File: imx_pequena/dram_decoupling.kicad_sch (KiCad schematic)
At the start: 19 parts

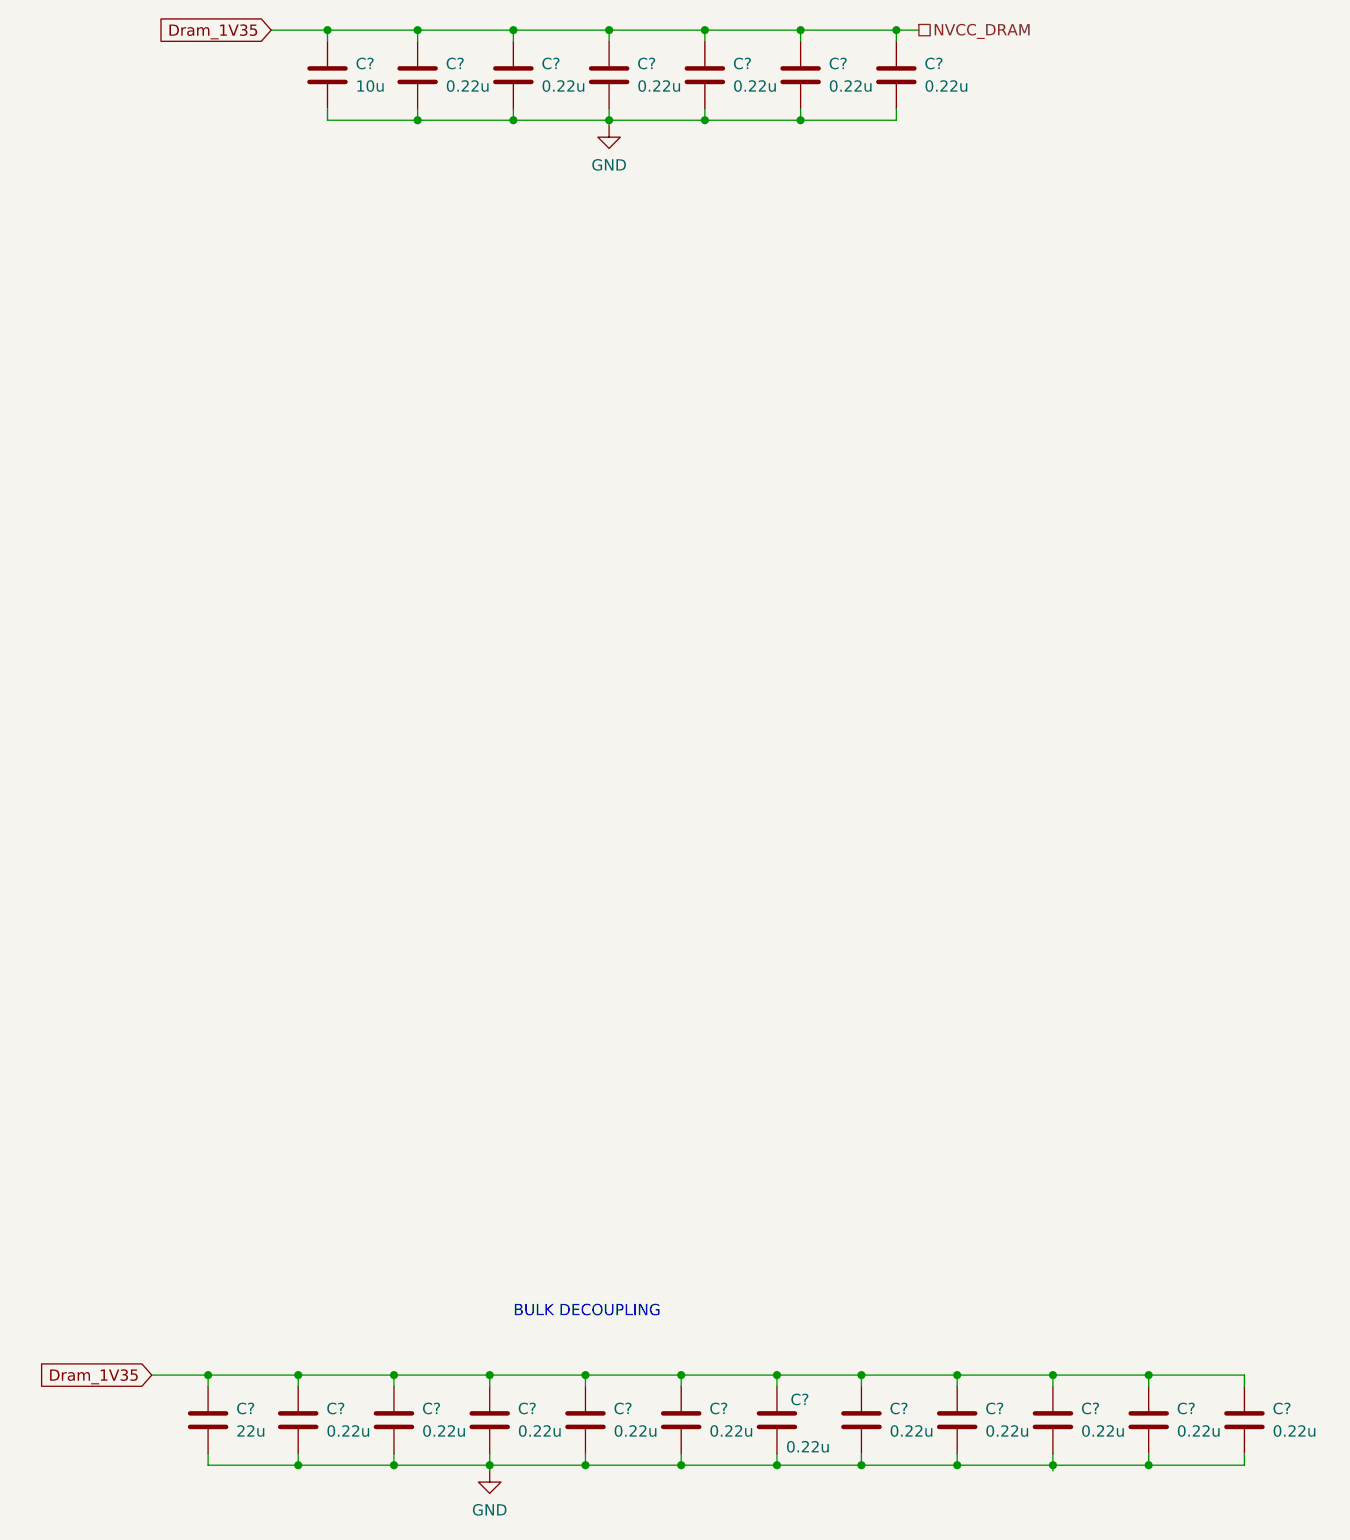
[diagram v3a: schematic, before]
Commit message: Power Update
Added 3v3 and 1.35V switchers
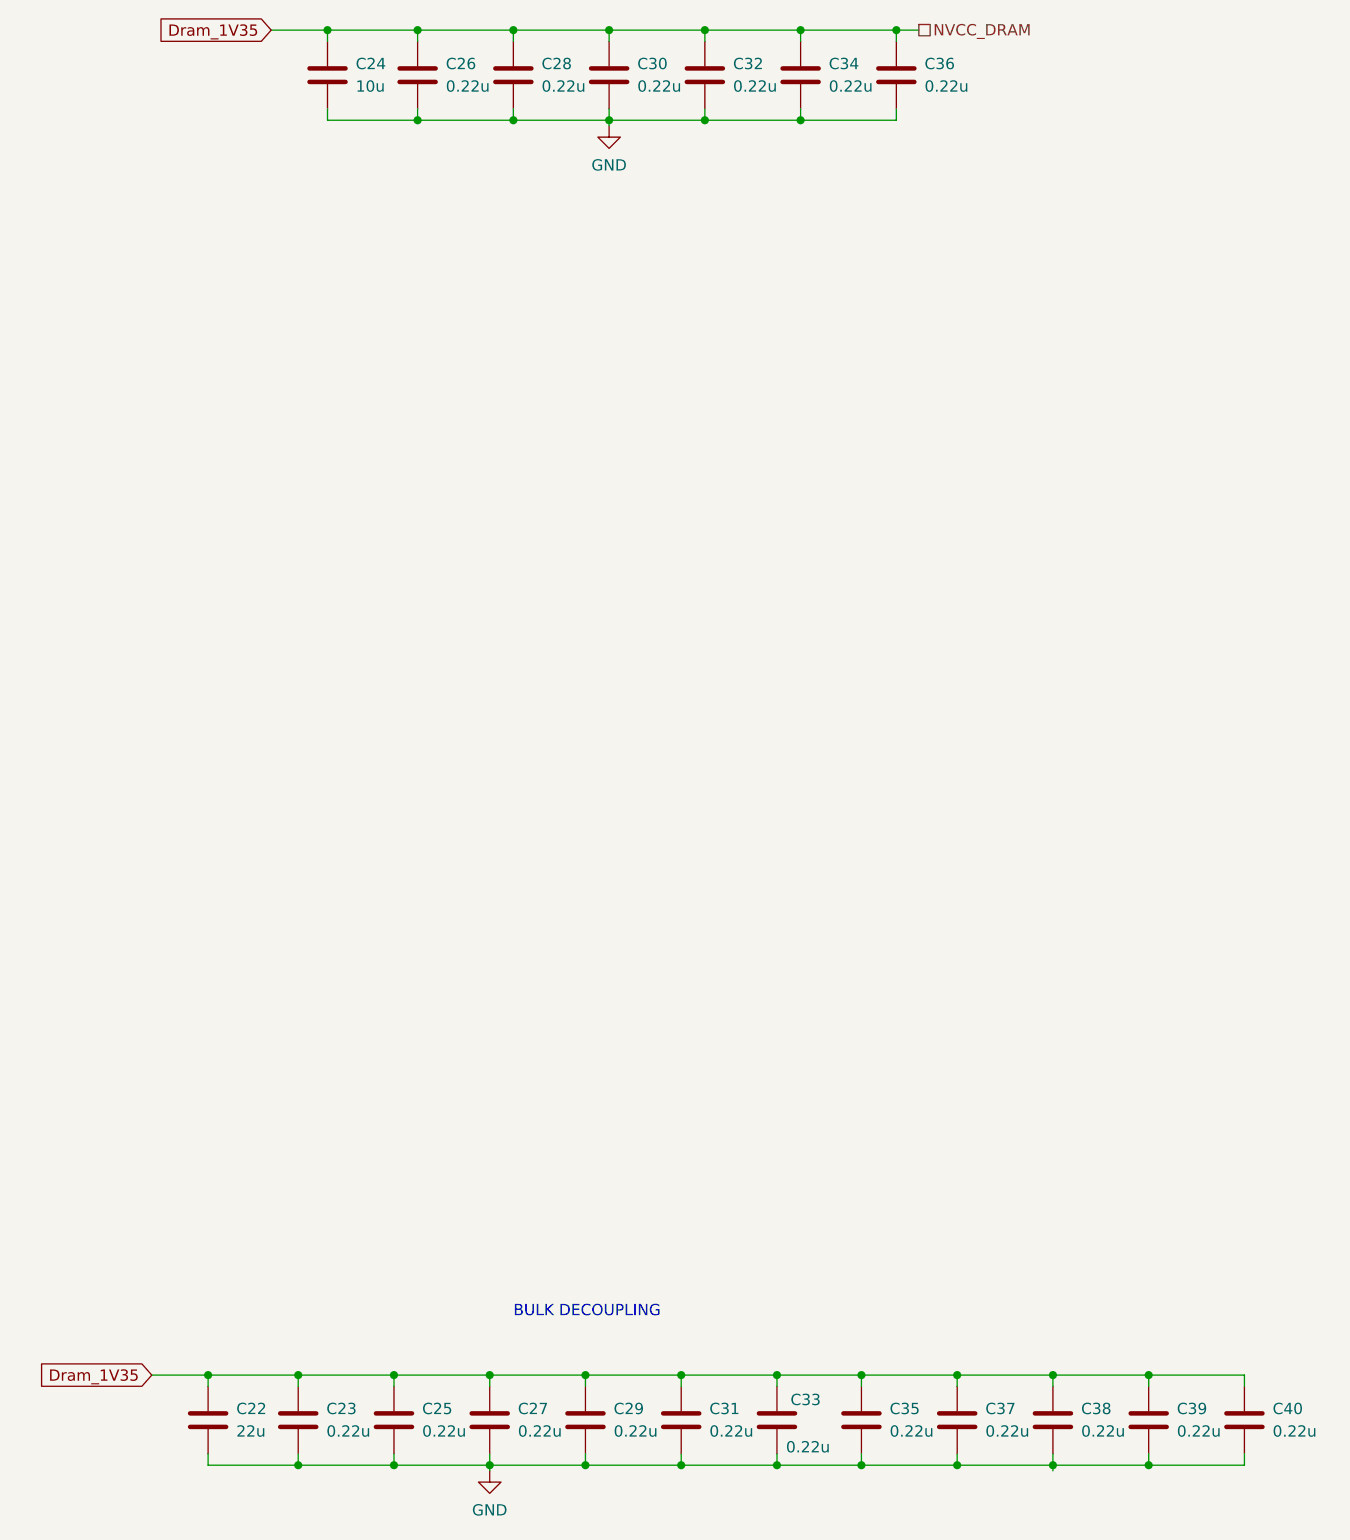
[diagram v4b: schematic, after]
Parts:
- gave numbers to parts that had none: 19
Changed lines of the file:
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@@
   (symbol (lib_id "Device:C") (at 55.118 184.658 0) (unit 1)
     (in_bom yes) (on_board yes) (fields_autoplaced)
-    (property "Reference" "C?" (id 0) (at 58.293 183.3879 0)
+    (property "Reference" "C25" (id 0) (at 58.293 183.3879 0)
       (effects (font (size 1.27 1.27)) (justify left))
     )
@@
   (symbol (lib_id "Device:C") (at 79.375 33.02 0) (unit 1)
     (in_bom yes) (on_board yes) (fields_autoplaced)
-    (property "Reference" "C?" (id 0) (at 82.55 31.7499 0)
+    (property "Reference" "C30" (id 0) (at 82.55 31.7499 0)
       (effects (font (size 1.27 1.27)) (justify left))
     )
@@
   (symbol (lib_id "Device:C") (at 76.708 184.658 0) (unit 1)
     (in_bom yes) (on_board yes) (fields_autoplaced)
-    (property "Reference" "C?" (id 0) (at 79.883 183.3879 0)
+    (property "Reference" "C29" (id 0) (at 79.883 183.3879 0)
       (effects (font (size 1.27 1.27)) (justify left))
     )
@@
   (symbol (lib_id "Device:C") (at 90.17 33.02 0) (unit 1)
     (in_bom yes) (on_board yes) (fields_autoplaced)
-    (property "Reference" "C?" (id 0) (at 93.345 31.7499 0)
+    (property "Reference" "C32" (id 0) (at 93.345 31.7499 0)
       (effects (font (size 1.27 1.27)) (justify left))
     )
@@
   (symbol (lib_id "power:GND") (at 65.913 190.373 0) (unit 1)
     (in_bom yes) (on_board yes) (fields_autoplaced)
-    (property "Reference" "#PWR?" (id 0) (at 65.913 196.723 0)
+    (property "Reference" "#PWR0122" (id 0) (at 65.913 196.723 0)
       (effects (font (size 1.27 1.27)) hide)
     )
@@
   (symbol (lib_id "Device:C") (at 65.913 184.658 0) (unit 1)
     (in_bom yes) (on_board yes) (fields_autoplaced)
-    (property "Reference" "C?" (id 0) (at 69.088 183.3879 0)
+    (property "Reference" "C27" (id 0) (at 69.088 183.3879 0)
       (effects (font (size 1.27 1.27)) (justify left))
     )
@@
   (symbol (lib_id "power:GND") (at 79.375 38.735 0) (unit 1)
     (in_bom yes) (on_board yes) (fields_autoplaced)
-    (property "Reference" "#PWR?" (id 0) (at 79.375 45.085 0)
+    (property "Reference" "#PWR0121" (id 0) (at 79.375 45.085 0)
       (effects (font (size 1.27 1.27)) hide)
     )
@@
   (symbol (lib_id "Device:C") (at 129.413 184.658 0) (unit 1)
     (in_bom yes) (on_board yes) (fields_autoplaced)
-    (property "Reference" "C?" (id 0) (at 132.588 183.3879 0)
+    (property "Reference" "C38" (id 0) (at 132.588 183.3879 0)
       (effects (font (size 1.27 1.27)) (justify left))
     )
@@
   (symbol (lib_id "Device:C") (at 151.003 184.658 0) (unit 1)
     (in_bom yes) (on_board yes) (fields_autoplaced)
-    (property "Reference" "C?" (id 0) (at 154.178 183.3879 0)
+    (property "Reference" "C40" (id 0) (at 154.178 183.3879 0)
       (effects (font (size 1.27 1.27)) (justify left))
     )
@@
   (symbol (lib_id "Device:C") (at 98.298 184.658 0) (unit 1)
     (in_bom yes) (on_board yes)
-    (property "Reference" "C?" (id 0) (at 99.822 182.372 0)
+    (property "Reference" "C33" (id 0) (at 99.822 182.372 0)
       (effects (font (size 1.27 1.27)) (justify left))
     )
@@
   (symbol (lib_id "Device:C") (at 111.76 33.02 0) (unit 1)
     (in_bom yes) (on_board yes) (fields_autoplaced)
-    (property "Reference" "C?" (id 0) (at 114.935 31.7499 0)
+    (property "Reference" "C36" (id 0) (at 114.935 31.7499 0)
       (effects (font (size 1.27 1.27)) (justify left))
     )
@@
   (symbol (lib_id "Device:C") (at 107.823 184.658 0) (unit 1)
     (in_bom yes) (on_board yes) (fields_autoplaced)
-    (property "Reference" "C?" (id 0) (at 110.998 183.3879 0)
+    (property "Reference" "C35" (id 0) (at 110.998 183.3879 0)
       (effects (font (size 1.27 1.27)) (justify left))
     )
@@
   (symbol (lib_id "Device:C") (at 47.625 33.02 0) (unit 1)
     (in_bom yes) (on_board yes) (fields_autoplaced)
-    (property "Reference" "C?" (id 0) (at 50.8 31.7499 0)
+    (property "Reference" "C24" (id 0) (at 50.8 31.7499 0)
       (effects (font (size 1.27 1.27)) (justify left))
     )
@@
   (symbol (lib_id "Device:C") (at 140.208 184.658 0) (unit 1)
     (in_bom yes) (on_board yes) (fields_autoplaced)
-    (property "Reference" "C?" (id 0) (at 143.383 183.3879 0)
+    (property "Reference" "C39" (id 0) (at 143.383 183.3879 0)
       (effects (font (size 1.27 1.27)) (justify left))
     )
@@
   (symbol (lib_id "Device:C") (at 87.503 184.658 0) (unit 1)
     (in_bom yes) (on_board yes) (fields_autoplaced)
-    (property "Reference" "C?" (id 0) (at 90.678 183.3879 0)
+    (property "Reference" "C31" (id 0) (at 90.678 183.3879 0)
       (effects (font (size 1.27 1.27)) (justify left))
     )
@@
   (symbol (lib_id "Device:C") (at 68.58 33.02 0) (unit 1)
     (in_bom yes) (on_board yes) (fields_autoplaced)
-    (property "Reference" "C?" (id 0) (at 71.755 31.7499 0)
+    (property "Reference" "C28" (id 0) (at 71.755 31.7499 0)
       (effects (font (size 1.27 1.27)) (justify left))
     )
@@
   (symbol (lib_id "Device:C") (at 57.785 33.02 0) (unit 1)
     (in_bom yes) (on_board yes) (fields_autoplaced)
-    (property "Reference" "C?" (id 0) (at 60.96 31.7499 0)
+    (property "Reference" "C26" (id 0) (at 60.96 31.7499 0)
       (effects (font (size 1.27 1.27)) (justify left))
     )
@@
   (symbol (lib_id "Device:C") (at 100.965 33.02 0) (unit 1)
     (in_bom yes) (on_board yes) (fields_autoplaced)
-    (property "Reference" "C?" (id 0) (at 104.14 31.7499 0)
+    (property "Reference" "C34" (id 0) (at 104.14 31.7499 0)
       (effects (font (size 1.27 1.27)) (justify left))
     )
@@
   (symbol (lib_id "Device:C") (at 34.163 184.658 0) (unit 1)
     (in_bom yes) (on_board yes) (fields_autoplaced)
-    (property "Reference" "C?" (id 0) (at 37.338 183.3879 0)
+    (property "Reference" "C22" (id 0) (at 37.338 183.3879 0)
       (effects (font (size 1.27 1.27)) (justify left))
     )
@@
   (symbol (lib_id "Device:C") (at 118.618 184.658 0) (unit 1)
     (in_bom yes) (on_board yes) (fields_autoplaced)
-    (property "Reference" "C?" (id 0) (at 121.793 183.3879 0)
+    (property "Reference" "C37" (id 0) (at 121.793 183.3879 0)
       (effects (font (size 1.27 1.27)) (justify left))
     )
@@
   (symbol (lib_id "Device:C") (at 44.323 184.658 0) (unit 1)
     (in_bom yes) (on_board yes) (fields_autoplaced)
-    (property "Reference" "C?" (id 0) (at 47.498 183.3879 0)
-      (effects (font (size 1.27 1.27)) (justify left))
-    )
+    (property "Reference" "C23" (id 0) (at 47.498 183.3879 0)
+      (effects (font (size 1.27 1.27)) (justify left))
+    )

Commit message: Part Assignment
Assigned GPIOs and assigned footprints to most parts
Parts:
- C22, C24: footprint (none) -> Capacitor_SMD:C_0805_2012Metric
- C23, C25, C26, C27, C28, C29, C30, C31, C32, C33, C34, C35, C36, C37, C38, C39, C40: footprint (none) -> Capacitor_SMD:C_0402_1005Metric
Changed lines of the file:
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@@
       (effects (font (size 1.27 1.27)) (justify left))
     )
-    (property "Footprint" "" (id 2) (at 56.0832 188.468 0)
+    (property "Footprint" "Capacitor_SMD:C_0402_1005Metric" (id 2) (at 56.0832 188.468 0)
       (effects (font (size 1.27 1.27)) hide)
     )
@@
       (effects (font (size 1.27 1.27)) (justify left))
     )
-    (property "Footprint" "" (id 2) (at 80.3402 36.83 0)
+    (property "Footprint" "Capacitor_SMD:C_0402_1005Metric" (id 2) (at 80.3402 36.83 0)
       (effects (font (size 1.27 1.27)) hide)
     )
@@
       (effects (font (size 1.27 1.27)) (justify left))
     )
-    (property "Footprint" "" (id 2) (at 77.6732 188.468 0)
+    (property "Footprint" "Capacitor_SMD:C_0402_1005Metric" (id 2) (at 77.6732 188.468 0)
       (effects (font (size 1.27 1.27)) hide)
     )
@@
       (effects (font (size 1.27 1.27)) (justify left))
     )
-    (property "Footprint" "" (id 2) (at 91.1352 36.83 0)
+    (property "Footprint" "Capacitor_SMD:C_0402_1005Metric" (id 2) (at 91.1352 36.83 0)
       (effects (font (size 1.27 1.27)) hide)
     )
@@
       (effects (font (size 1.27 1.27)) (justify left))
     )
-    (property "Footprint" "" (id 2) (at 66.8782 188.468 0)
+    (property "Footprint" "Capacitor_SMD:C_0402_1005Metric" (id 2) (at 66.8782 188.468 0)
       (effects (font (size 1.27 1.27)) hide)
     )
@@
       (effects (font (size 1.27 1.27)) (justify left))
     )
-    (property "Footprint" "" (id 2) (at 130.3782 188.468 0)
+    (property "Footprint" "Capacitor_SMD:C_0402_1005Metric" (id 2) (at 130.3782 188.468 0)
       (effects (font (size 1.27 1.27)) hide)
     )
@@
       (effects (font (size 1.27 1.27)) (justify left))
     )
-    (property "Footprint" "" (id 2) (at 151.9682 188.468 0)
+    (property "Footprint" "Capacitor_SMD:C_0402_1005Metric" (id 2) (at 151.9682 188.468 0)
       (effects (font (size 1.27 1.27)) hide)
     )
@@
       (effects (font (size 1.27 1.27)) (justify left))
     )
-    (property "Footprint" "" (id 2) (at 99.2632 188.468 0)
+    (property "Footprint" "Capacitor_SMD:C_0402_1005Metric" (id 2) (at 99.2632 188.468 0)
       (effects (font (size 1.27 1.27)) hide)
     )
@@
       (effects (font (size 1.27 1.27)) (justify left))
     )
-    (property "Footprint" "" (id 2) (at 112.7252 36.83 0)
+    (property "Footprint" "Capacitor_SMD:C_0402_1005Metric" (id 2) (at 112.7252 36.83 0)
       (effects (font (size 1.27 1.27)) hide)
     )
@@
       (effects (font (size 1.27 1.27)) (justify left))
     )
-    (property "Footprint" "" (id 2) (at 108.7882 188.468 0)
+    (property "Footprint" "Capacitor_SMD:C_0402_1005Metric" (id 2) (at 108.7882 188.468 0)
       (effects (font (size 1.27 1.27)) hide)
     )
@@
       (effects (font (size 1.27 1.27)) (justify left))
     )
-    (property "Footprint" "" (id 2) (at 48.5902 36.83 0)
+    (property "Footprint" "Capacitor_SMD:C_0805_2012Metric" (id 2) (at 48.5902 36.83 0)
       (effects (font (size 1.27 1.27)) hide)
     )
@@
       (effects (font (size 1.27 1.27)) (justify left))
     )
-    (property "Footprint" "" (id 2) (at 141.1732 188.468 0)
+    (property "Footprint" "Capacitor_SMD:C_0402_1005Metric" (id 2) (at 141.1732 188.468 0)
       (effects (font (size 1.27 1.27)) hide)
     )
@@
       (effects (font (size 1.27 1.27)) (justify left))
     )
-    (property "Footprint" "" (id 2) (at 88.4682 188.468 0)
+    (property "Footprint" "Capacitor_SMD:C_0402_1005Metric" (id 2) (at 88.4682 188.468 0)
       (effects (font (size 1.27 1.27)) hide)
     )
@@
       (effects (font (size 1.27 1.27)) (justify left))
     )
-    (property "Footprint" "" (id 2) (at 69.5452 36.83 0)
+    (property "Footprint" "Capacitor_SMD:C_0402_1005Metric" (id 2) (at 69.5452 36.83 0)
       (effects (font (size 1.27 1.27)) hide)
     )
@@
       (effects (font (size 1.27 1.27)) (justify left))
     )
-    (property "Footprint" "" (id 2) (at 58.7502 36.83 0)
+    (property "Footprint" "Capacitor_SMD:C_0402_1005Metric" (id 2) (at 58.7502 36.83 0)
       (effects (font (size 1.27 1.27)) hide)
     )
@@
       (effects (font (size 1.27 1.27)) (justify left))
     )
-    (property "Footprint" "" (id 2) (at 101.9302 36.83 0)
+    (property "Footprint" "Capacitor_SMD:C_0402_1005Metric" (id 2) (at 101.9302 36.83 0)
       (effects (font (size 1.27 1.27)) hide)
     )
@@
       (effects (font (size 1.27 1.27)) (justify left))
     )
-    (property "Footprint" "" (id 2) (at 35.1282 188.468 0)
+    (property "Footprint" "Capacitor_SMD:C_0805_2012Metric" (id 2) (at 35.1282 188.468 0)
       (effects (font (size 1.27 1.27)) hide)
     )
@@
       (effects (font (size 1.27 1.27)) (justify left))
     )
-    (property "Footprint" "" (id 2) (at 119.5832 188.468 0)
+    (property "Footprint" "Capacitor_SMD:C_0402_1005Metric" (id 2) (at 119.5832 188.468 0)
       (effects (font (size 1.27 1.27)) hide)
     )
@@
       (effects (font (size 1.27 1.27)) (justify left))
     )
-    (property "Footprint" "" (id 2) (at 45.2882 188.468 0)
-      (effects (font (size 1.27 1.27)) hide)
-    )
+    (property "Footprint" "Capacitor_SMD:C_0402_1005Metric" (id 2) (at 45.2882 188.468 0)
+      (effects (font (size 1.27 1.27)) hide)
+    )
